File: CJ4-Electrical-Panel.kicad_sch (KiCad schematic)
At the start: 43 parts, among them J1 Conn_01x03, J2 Conn_01x03, J3 Conn_01x03, J4 Conn_01x03, J5 Conn_01x03, J6 Conn_01x03, J7 USB_B_Micro, J8 AVR-ISP-6, U1 ATmega32U4-A, Y1 16MHz

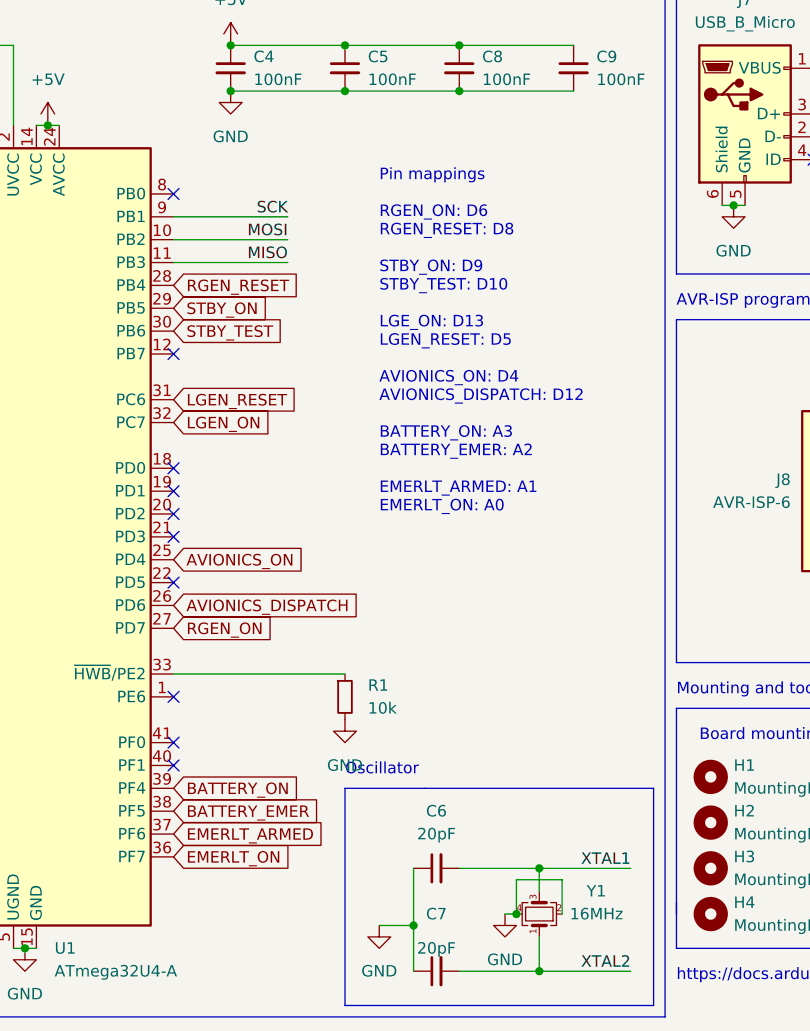
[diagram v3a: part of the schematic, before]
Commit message: Fixes Make switch holes bigger #2
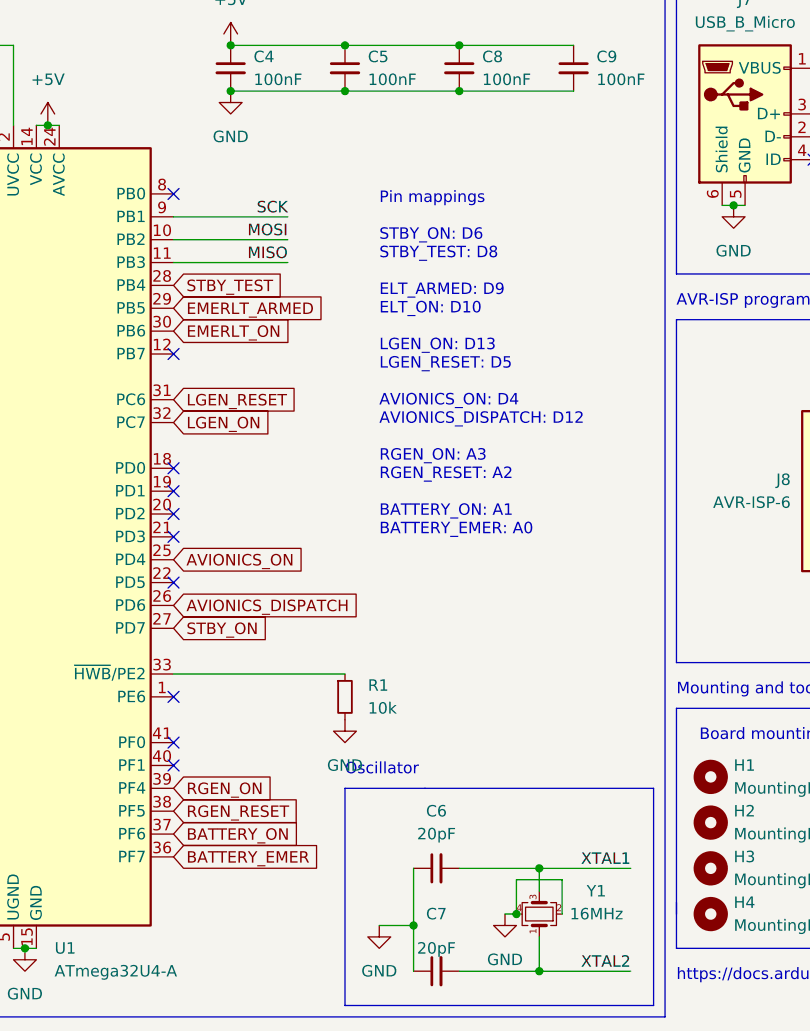
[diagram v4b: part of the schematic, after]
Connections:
- net BATTERY_EMER: now also U1.36 (PF7); no longer U1.38 (PF5)
- net BATTERY_ON: now also U1.37 (PF6); no longer U1.39 (PF4)
- net EMERLT_ARMED: now also U1.29 (PB5); no longer U1.37 (PF6)
- net EMERLT_ON: now also U1.30 (PB6); no longer U1.36 (PF7)
- net RGEN_ON: now also U1.39 (PF4); no longer U1.27 (PD7)
- net RGEN_RESET: now also U1.38 (PF5); no longer U1.28 (PB4)
- net STBY_ON: now also U1.27 (PD7); no longer U1.29 (PB5)
- net STBY_TEST: now also U1.28 (PB4); no longer U1.30 (PB6)
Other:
- note added: "Pin mappings STBY_ON: D6 STBY_TEST: D8 ELT_ARMED: D9 ELT_ON: D10 LGEN_ON: D13 LGEN_RESET: D5 AVIONICS_ON: D4 AVIONICS_DISPATCH: D12 RGEN_ON: A3 RGEN_RESET: A2 BATTERY_ON: A1 BATTERY_EMER: A0"
- note removed: "Pin mappings RGEN_ON: D6 RGEN_RESET: D8 STBY_ON: D9 STBY_TEST: D10 LGE_ON: D13 LGEN_RESET: D5 AVIONICS_ON: D4 AVIONICS_DISPATCH: D12 BATTERY_ON: A3 BATTERY_EMER: A2 EMERLT_ARMED: A1 EMERLT_ON: A0"
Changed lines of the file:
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@@
     (effects (font (size 1.27 1.27)) (justify left bottom))
   )
-  (text "Pin mappings\n\nRGEN_ON: D6\nRGEN_RESET: D8\n\nSTBY_ON: D9\nSTBY_TEST: D10\n\nLGE_ON: D13\nLGEN_RESET: D5\n\nAVIONICS_ON: D4\nAVIONICS_DISPATCH: D12\n\nBATTERY_ON: A3\nBATTERY_EMER: A2\n\nEMERLT_ARMED: A1\nEMERLT_ON: A0"
-    (at 86.36 76.2 0)
+  (text "Pin mappings\n\nSTBY_ON: D6\nSTBY_TEST: D8\n\nELT_ARMED: D9\nELT_ON: D10\n\nLGEN_ON: D13\nLGEN_RESET: D5\n\nAVIONICS_ON: D4\nAVIONICS_DISPATCH: D12\n\nRGEN_ON: A3\nRGEN_RESET: A2\n\nBATTERY_ON: A1\nBATTERY_EMER: A0"
+    (at 86.36 78.74 0)
     (effects (font (size 1.27 1.27)) (justify left bottom))
   )
@@
     )
   )
-  (global_label "STBY_TEST" (shape input) (at 63.5 55.88 0) (fields_autoplaced)
-    (effects (font (size 1.27 1.27)) (justify left))
-    (property "Intersheet References" "${INTERSHEET_REFS}" (id 0) (at 75.7102 55.8006 0)
+  (global_label "STBY_TEST" (shape input) (at 63.5 50.8 0) (fields_autoplaced)
+    (effects (font (size 1.27 1.27)) (justify left))
+    (property "Intersheet References" "${INTERSHEET_REFS}" (id 0) (at 75.7102 50.7206 0)
       (effects (font (size 1.27 1.27)) (justify left) hide)
     )
@@
     )
   )
-  (global_label "STBY_ON" (shape input) (at 63.5 53.34 0) (fields_autoplaced)
-    (effects (font (size 1.27 1.27)) (justify left))
-    (property "Intersheet References" "${INTERSHEET_REFS}" (id 0) (at 74.0774 53.2606 0)
+  (global_label "STBY_ON" (shape input) (at 63.5 88.9 0) (fields_autoplaced)
+    (effects (font (size 1.27 1.27)) (justify left))
+    (property "Intersheet References" "${INTERSHEET_REFS}" (id 0) (at 74.0774 88.8206 0)
       (effects (font (size 1.27 1.27)) (justify left) hide)
     )
@@
     )
   )
-  (global_label "RGEN_ON" (shape input) (at 63.5 88.9 0) (fields_autoplaced)
-    (effects (font (size 1.27 1.27)) (justify left))
-    (property "Intersheet References" "${INTERSHEET_REFS}" (id 0) (at 74.5612 88.8206 0)
-      (effects (font (size 1.27 1.27)) (justify left) hide)
-    )
-  )
-  (global_label "RGEN_RESET" (shape input) (at 63.5 50.8 0) (fields_autoplaced)
-    (effects (font (size 1.27 1.27)) (justify left))
-    (property "Intersheet References" "${INTERSHEET_REFS}" (id 0) (at 77.6455 50.7206 0)
+  (global_label "RGEN_ON" (shape input) (at 63.5 106.68 0) (fields_autoplaced)
+    (effects (font (size 1.27 1.27)) (justify left))
+    (property "Intersheet References" "${INTERSHEET_REFS}" (id 0) (at 74.5612 106.6006 0)
+      (effects (font (size 1.27 1.27)) (justify left) hide)
+    )
+  )
+  (global_label "RGEN_RESET" (shape input) (at 63.5 109.22 0) (fields_autoplaced)
+    (effects (font (size 1.27 1.27)) (justify left))
+    (property "Intersheet References" "${INTERSHEET_REFS}" (id 0) (at 77.6455 109.1406 0)
       (effects (font (size 1.27 1.27)) (justify left) hide)
     )
@@
     )
   )
-  (global_label "EMERLT_ARMED" (shape input) (at 63.5 111.76 0) (fields_autoplaced)
-    (effects (font (size 1.27 1.27)) (justify left))
-    (property "Intersheet References" "${INTERSHEET_REFS}" (id 0) (at 80.125 111.6806 0)
-      (effects (font (size 1.27 1.27)) (justify left) hide)
-    )
-  )
-  (global_label "BATTERY_ON" (shape input) (at 63.5 106.68 0) (fields_autoplaced)
-    (effects (font (size 1.27 1.27)) (justify left))
-    (property "Intersheet References" "${INTERSHEET_REFS}" (id 0) (at 77.3431 106.6006 0)
+  (global_label "EMERLT_ARMED" (shape input) (at 63.5 53.34 0) (fields_autoplaced)
+    (effects (font (size 1.27 1.27)) (justify left))
+    (property "Intersheet References" "${INTERSHEET_REFS}" (id 0) (at 80.125 53.2606 0)
+      (effects (font (size 1.27 1.27)) (justify left) hide)
+    )
+  )
+  (global_label "BATTERY_ON" (shape input) (at 63.5 111.76 0) (fields_autoplaced)
+    (effects (font (size 1.27 1.27)) (justify left))
+    (property "Intersheet References" "${INTERSHEET_REFS}" (id 0) (at 77.3431 111.6806 0)
       (effects (font (size 1.27 1.27)) (justify left) hide)
     )
@@
     )
   )
-  (global_label "BATTERY_EMER" (shape input) (at 63.5 109.22 0) (fields_autoplaced)
-    (effects (font (size 1.27 1.27)) (justify left))
-    (property "Intersheet References" "${INTERSHEET_REFS}" (id 0) (at 79.7017 109.1406 0)
+  (global_label "BATTERY_EMER" (shape input) (at 63.5 114.3 0) (fields_autoplaced)
+    (effects (font (size 1.27 1.27)) (justify left))
+    (property "Intersheet References" "${INTERSHEET_REFS}" (id 0) (at 79.7017 114.2206 0)
       (effects (font (size 1.27 1.27)) (justify left) hide)
     )
@@
     )
   )
-  (global_label "EMERLT_ON" (shape input) (at 63.5 114.3 0) (fields_autoplaced)
-    (effects (font (size 1.27 1.27)) (justify left))
-    (property "Intersheet References" "${INTERSHEET_REFS}" (id 0) (at 76.5569 114.2206 0)
-      (effects (font (size 1.27 1.27)) (justify left) hide)
-    )
+  (global_label "EMERLT_ON" (shape input) (at 63.5 55.88 0) (fields_autoplaced)
+    (effects (font (size 1.27 1.27)) (justify left))
+    (property "Intersheet References" "${INTERSHEET_REFS}" (id 0) (at 76.5569 55.8006 0)
+      (effects (font (size 1.27 1.27)) (justify left) hide)
+    )

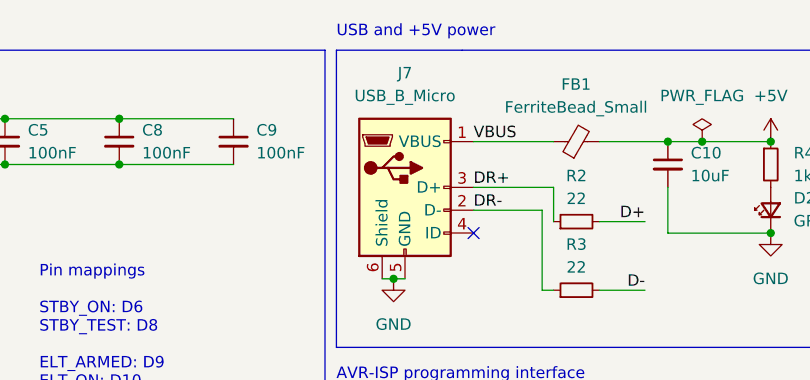
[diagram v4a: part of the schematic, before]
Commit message: Replace USB connector Fixes #1
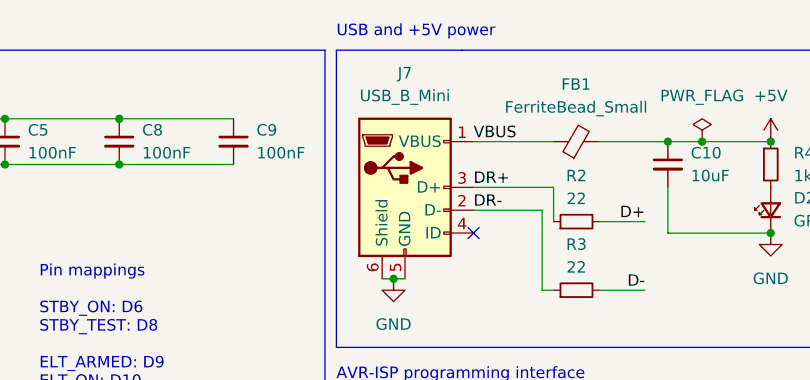
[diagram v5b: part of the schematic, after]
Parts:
- removed J7: USB_B_Micro, CJ4-Electrical-Panel:USB_B_Mini_Amphenol_UE25BE5510H, symbol Connector:USB_B_Micro
- added J7: USB_B_Mini, CJ4-Electrical-Panel:USB_B_Mini_Amphenol_UE25BE5510H, symbol Connector:USB_B_Mini
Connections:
- net DR+: now also J7.3 (D+)
- net DR-: now also J7.2 (D-)
- net GND: now also J7.5 (GND), J7.6 (Shield)
- net VBUS: now also J7.1 (VBUS)
